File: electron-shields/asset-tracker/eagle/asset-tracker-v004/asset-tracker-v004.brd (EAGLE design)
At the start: 57.1 x 57.1 mm, 23 parts, among them J1 1X2-3.5MM, T1 DMG3415, U1 PAM-7Q-GPS-TH, U3 LIS3DHTR, X1 ELECTRON

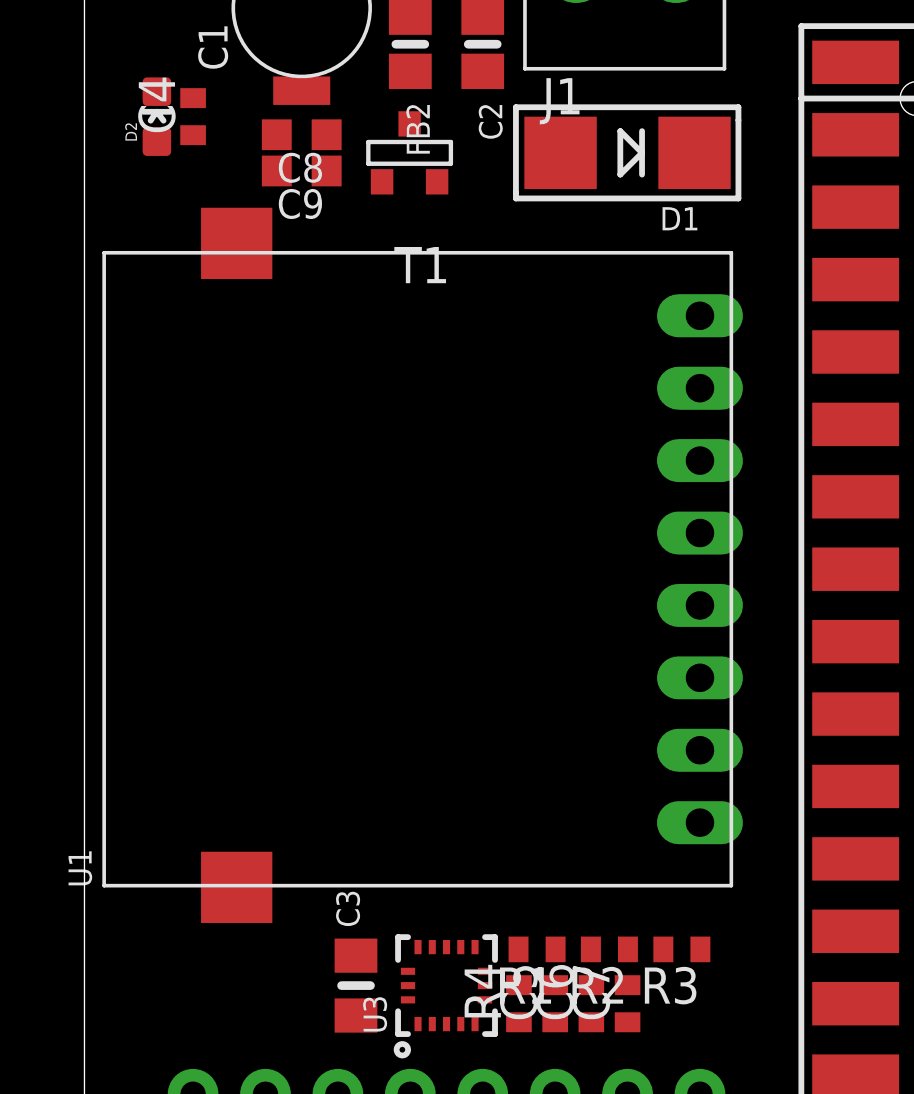
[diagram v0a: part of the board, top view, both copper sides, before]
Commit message: added max-m8 gps and max2674 ant switch packages
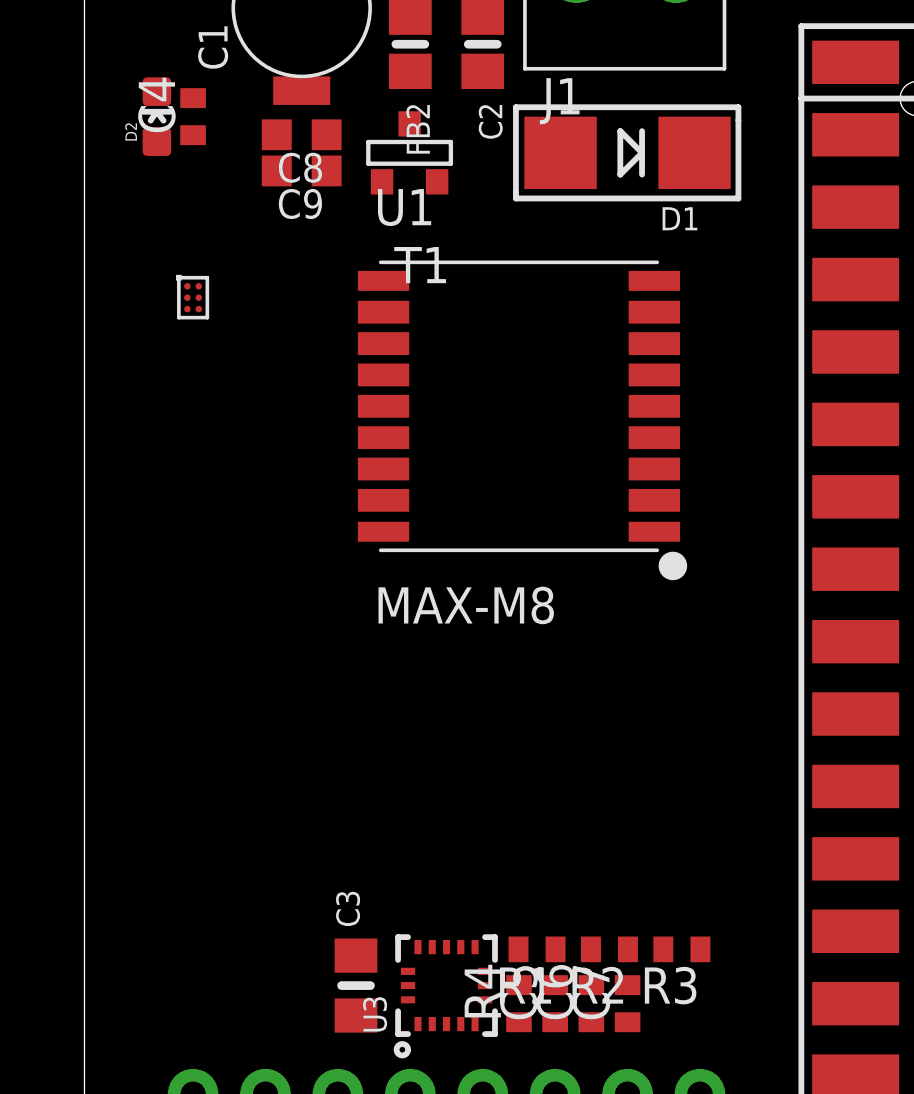
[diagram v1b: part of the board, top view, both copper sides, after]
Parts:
- added U2: MAX2674, maxim:WLP-6
- U1: value PAM-7Q-GPS-TH -> MAX-M8; device u-blox:PAM-7Q-TH -> u-blox:MAX-M8
- moved U1 15.9 mm to (15.2, 38.1), turned to 0 degrees
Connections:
- removed net V_BKP: U1.5
- new net GNDAC: U2.B2
- new net GNDDC: U2.C1
- net GND: no longer U1.3
- net VCC: now also U2.A1; no longer U1.4
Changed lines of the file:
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@@
 </autorouter>
 <elements>
-<element name="U1" library="u-blox" package="PAM-7Q-TH" value="PAM-7Q-GPS-TH" x="21.59" y="23.495" rot="R90"/>
 <element name="C1" library="adafruit" package="414-VA5R" value="" x="7.62" y="52.07" rot="R90"/>
 <element name="U3" library="microbuilder" package="LGA16_3X3MM" value="LIS3DHTR" x="12.7" y="17.78" rot="R90"/>
@@
 <element name="C8" library="rcl" package="C0603K" value="" x="7.62" y="47.625" rot="R180"/>
 <element name="C9" library="rcl" package="C0603K" value="" x="7.62" y="46.355" rot="R180"/>
+<element name="U1" library="u-blox" package="MAX-M8" value="MAX-M8" x="15.24" y="38.1"/>
+<element name="U2" library="maxim" package="WLP-6" value="MAX2674" x="3.81" y="41.91"/>
 </elements>
 <signals>
 <signal name="GND">
-<contactref element="U1" pad="3"/>
 <contactref element="U3" pad="5"/>
 <contactref element="U3" pad="10"/>
@@
 <contactref element="X1" pad="33B"/>
 <contactref element="X1" pad="33C"/>
-<wire x1="13.2" y1="19.13" x2="21.59" y2="28.575" width="0" layer="19" extent="1-1"/>
-<wire x1="12.2" y1="19.13" x2="13.2" y2="19.13" width="0" layer="19" extent="1-1"/>
-<wire x1="13.7" y1="16.43" x2="13.2" y2="19.13" width="0" layer="19" extent="1-1"/>
-<wire x1="9.525" y1="18.83" x2="13.7" y2="16.43" width="0" layer="19" extent="1-1"/>
-<wire x1="13.97" y1="49.85" x2="9.525" y2="18.83" width="0" layer="19" extent="1-1"/>
-<wire x1="17.25" y1="53.34" x2="13.97" y2="49.85" width="0" layer="19" extent="1-1"/>
-<wire x1="34.29" y1="47.625" x2="13.97" y2="49.85" width="0" layer="19" extent="1-1"/>
+<wire x1="47.371" y1="42.545" x2="51.689" y2="42.545" width="0" layer="19" extent="1-1"/>
+<wire x1="44.45" y1="42.545" x2="47.371" y2="42.545" width="0" layer="19" extent="1-1"/>
+<wire x1="34.29" y1="47.625" x2="44.45" y2="42.545" width="0" layer="19" extent="1-1"/>
 <wire x1="31.369" y1="47.625" x2="34.29" y2="47.625" width="0" layer="19" extent="1-1"/>
 <wire x1="27.051" y1="47.625" x2="31.369" y2="47.625" width="0" layer="19" extent="1-1"/>
-<wire x1="44.45" y1="42.545" x2="34.29" y2="47.625" width="0" layer="19" extent="1-1"/>
-<wire x1="47.371" y1="42.545" x2="44.45" y2="42.545" width="0" layer="19" extent="1-1"/>
-<wire x1="51.689" y1="42.545" x2="47.371" y2="42.545" width="0" layer="19" extent="1-1"/>
-</signal>
-<signal name="VCC">
-<contactref element="U1" pad="4"/>
-</signal>
-<signal name="V_BKP">
-<contactref element="U1" pad="5"/>
+<wire x1="17.25" y1="53.34" x2="27.051" y2="47.625" width="0" layer="19" extent="1-1"/>
+<wire x1="13.97" y1="49.85" x2="17.25" y2="53.34" width="0" layer="19" extent="1-1"/>
+<wire x1="13.2" y1="19.13" x2="13.97" y2="49.85" width="0" layer="19" extent="1-1"/>
+<wire x1="12.2" y1="19.13" x2="13.2" y2="19.13" width="0" layer="19" extent="1-1"/>
+<wire x1="9.525" y1="18.83" x2="12.2" y2="19.13" width="0" layer="19" extent="1-1"/>
+<wire x1="13.7" y1="16.43" x2="13.2" y2="19.13" width="0" layer="19" extent="1-1"/>
 </signal>
 <signal name="3.3V">
@@
 <wire x1="27.051" y1="50.165" x2="31.369" y2="50.165" width="0" layer="19" extent="1-1"/>
 </signal>
+<signal name="GNDAC">
+<contactref element="U2" pad="B2"/>
+</signal>
+<signal name="VCC">
+<contactref element="U2" pad="A1"/>
+</signal>
+<signal name="GNDDC">
+<contactref element="U2" pad="C1"/>
+</signal>
 </signals>

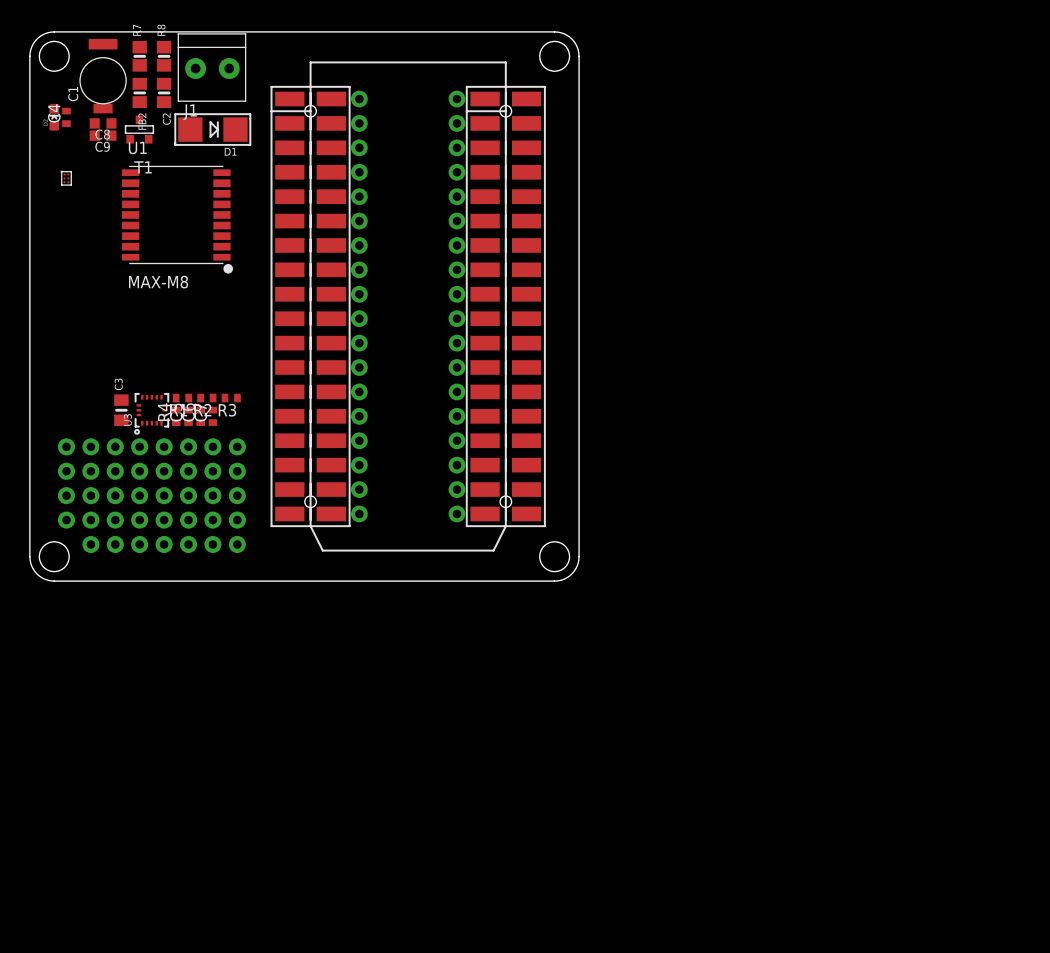
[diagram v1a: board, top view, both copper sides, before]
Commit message: updated schematic and added more data sheets
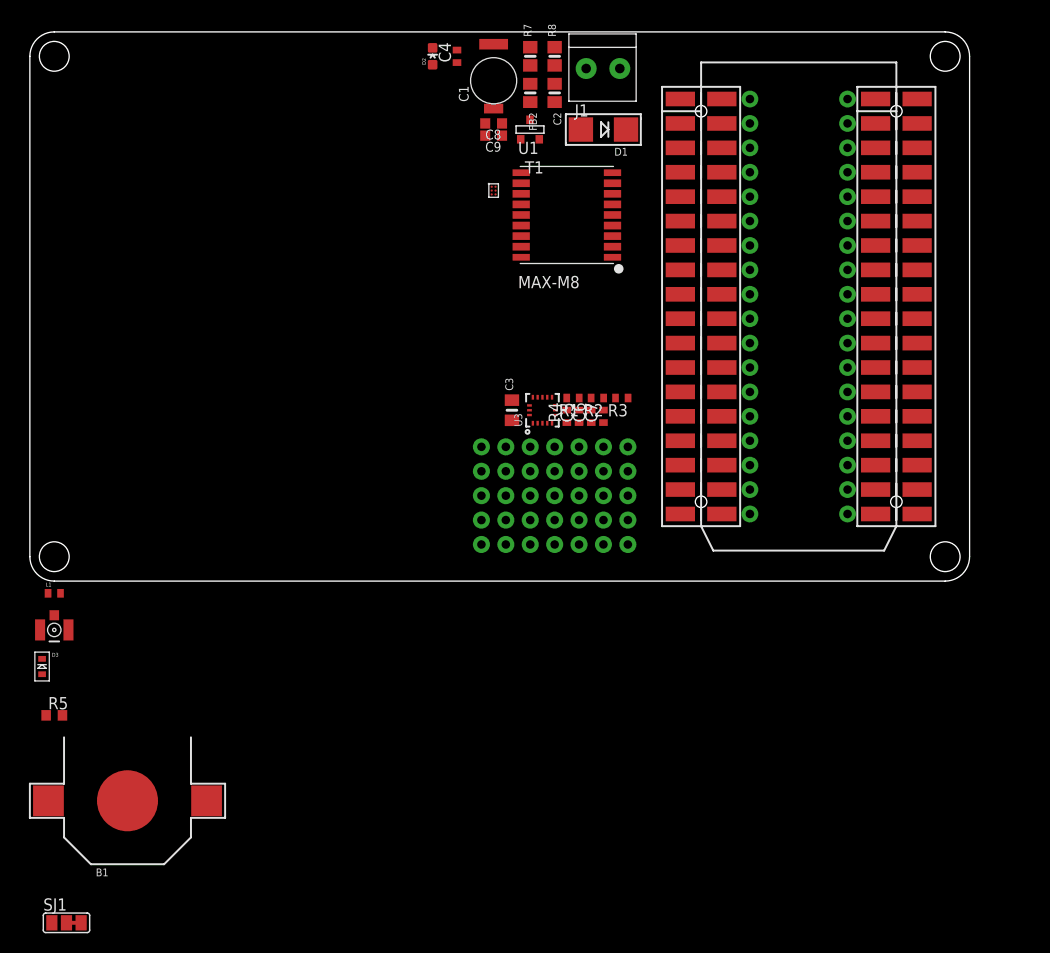
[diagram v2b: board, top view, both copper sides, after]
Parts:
- added B1: CR1220, microbuilder:CR1220
- added D3: (no value), adafruit:SOD-523
- added L1: (no value), Particle:C0402
- added R5: 270, rcl:R0603
- added SJ1: JUMPER-PAD-3-2OF3_NC_BY_TRACE_LARGE, SparkFun-Passives:PAD-JUMPER-3-2OF3_NC_BY_TRACE_YES_SILK_LARGE
- added X2: IPEX-20279-001E, Particle:IPEX-20279-001E
- C1: value (none) -> 60mF
- C5: value (none) -> 100pF
- moved U2 44.5 mm to (48.3, 40.6)
- moved C4 41.1 mm to (44.5, 54.6)
- moved X1 40.6 mm to (80.0, 28.6)
- moved C1 40.6 mm to (48.3, 52.1)
- moved C2 40.6 mm to (54.6, 50.8)
- moved C3 40.6 mm to (50.2, 17.8)
- moved C5 40.6 mm to (57.1, 17.1)
- moved C6 40.6 mm to (58.4, 17.1)
- moved C7 40.6 mm to (59.7, 17.1)
- moved C8 40.6 mm to (48.3, 47.6)
- moved C9 40.6 mm to (48.3, 46.4)
- moved D1 40.6 mm to (59.7, 47.0)
- moved FB2 40.6 mm to (52.1, 50.8)
- moved J1 40.6 mm to (59.7, 53.3)
- moved R1 40.6 mm to (56.5, 19.1)
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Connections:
- removed net 3V3: X1.36A, X1.36B, X1.36C
- removed net GNDAC: U2.B2
- removed net GNDDC: U2.C1
- removed net VCC: U2.A1
- removed net VIN: X1.1A, X1.1B, X1.1C
- new net GPS_!RESET: U1.9
- new net GPS_!SAFEBOOT: U1.18
- new net GPS_EXTINT: U1.5
- new net GPS_LNA_EN: U1.13
- new net GPS_PWR_EN: R7.1, T1.3, X1.31A, X1.31B, X1.31C
- new net GPS_RF_IN: C5.2, U1.11
- new net GPS_RXD: U1.3, X1.3A, X1.3B, X1.3C
- new net GPS_SCL: U1.17
- new net GPS_SDA: U1.16
- new net GPS_TXD: U1.2, X1.4A, X1.4B, X1.4C
- new net N$10: D3.K, R5.2
- new net N$11: B1.+$1, SJ1.1
- new net N$4: C5.1, U2.A2
- new net N$43: X1.6A, X1.6B, X1.6C
- new net N$48: X1.11A, X1.11B, X1.11C
- new net N$49: X1.12A, X1.12B, X1.12C
- new net N$5: U2.C2, X2.1
- new net N$57: X1.13A, X1.13B, X1.13C
- new net N$58: X1.14A, X1.14B, X1.14C
- new net N$59: X1.15A, X1.15B, X1.15C
- new net N$6: D2.C, R1.2
- new net N$60: X1.16A, X1.16B, X1.16C
- new net N$61: X1.17A, X1.17B, X1.17C
- new net N$62: X1.18A, X1.18B, X1.18C
- new net N$63: X1.19A, X1.19B, X1.19C
- new net N$64: X1.20A, X1.20B, X1.20C
- new net N$65: X1.21A, X1.21B, X1.21C
- new net N$66: X1.22A, X1.22B, X1.22C
- new net N$67: X1.23A, X1.23B, X1.23C
- new net N$68: X1.24A, X1.24B, X1.24C
- new net N$69: X1.25A, X1.25B, X1.25C
- new net N$7: C1.+, R5.1, SJ1.3
- new net N$70: X1.26A, X1.26B, X1.26C
- new net N$71: X1.27A, X1.27B, X1.27C
- new net N$72: X1.28A, X1.28B, X1.28C
- new net N$73: X1.29A, X1.29B, X1.29C
- new net N$74: X1.30A, X1.30B, X1.30C
- new net N$76: X1.32A, X1.32B, X1.32C
- new net N$78: X1.34A, X1.34B, X1.34C
- new net N$79: X1.35A, X1.35B, X1.35C
- new net TIMEPULSE: D2.A, U1.4
- new net VCC_RF: U1.14, U2.A1
- new net V_ANT: U1.15
- new net V_BCKP: SJ1.2, U1.6
- net 3.3V: now also D3.A, X1.36A, X1.36B, X1.36C
- net ACCEL_CS: now also X1.10A, X1.10B, X1.10C
- net ACCEL_INT1: now also X1.5A, X1.5B, X1.5C
- net ACCEL_MISO: now also X1.8A, X1.8B, X1.8C
- net ACCEL_MOSI: now also X1.7A, X1.7B, X1.7C
- net ACCEL_SCK: now also X1.9A, X1.9B, X1.9C
- net GND: now also B1.-, C1.-, C4.1, C9.1, R1.1, U1.1, U1.10, U1.12, U2.B2, U2.C1, X2.2@1, X2.2@2
- net N$1: now also C4.2, C9.2, U1.7, U1.8; no longer FB2.2
- net N$2: now also L1.2, U2.B1; no longer FB2.1
- net N$3: now also C6.2, L1.1; no longer R7.1, T1.3
- net N$8: now also X1.1A, X1.1B, X1.1C
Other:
- board size 57.1 x 57.1 mm -> 97.8 x 57.1 mm

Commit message: added patch antenna and enclosure outline
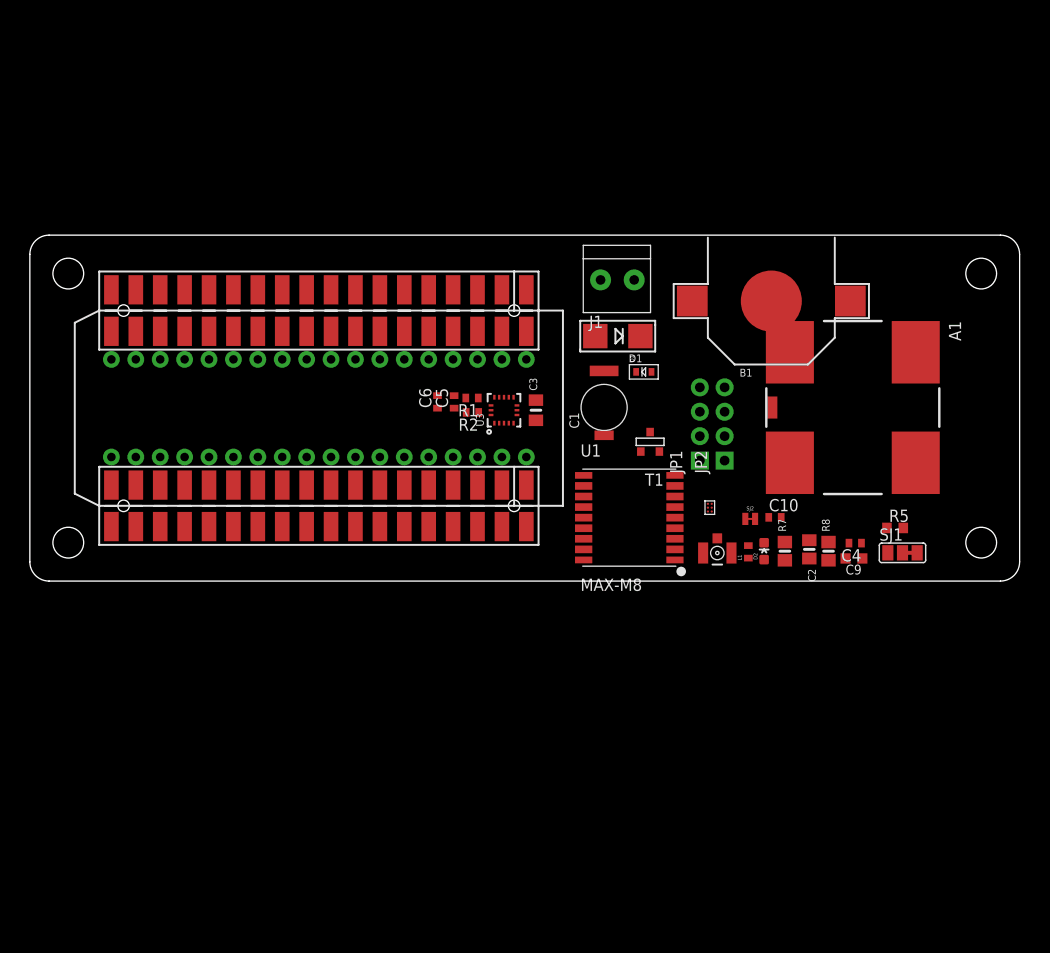
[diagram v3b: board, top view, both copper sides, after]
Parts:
- removed C7: (no value), rcl:C0402
- removed C8: (no value), rcl:C0603K
- removed FB2: Ferrite, microbuilder:0805-NO@1
- removed R3, R4: (no value), rcl:R0402
- added A1: GPS-ANTENNA, antenna:ANT1818B00BT1516S
- added C10: 0.1uF, rcl:C0402
- added JP1, JP2: (no value), SparkFun-Connectors:1X04_NO_SILK
- added SJ2: JUMPER-PAD-2-NC_BY_TRACENO_SILK, SparkFun-Passives:PAD-JUMPER-2-NC_BY_TRACE_NO_SILK
- C4: value (none) -> 0.1uF
- C6: value (none) -> 100pF
- C9: value (none) -> 10uF
- L1: value (none) -> 88nH
- R2: value (none) -> 100K
- moved SJ1 95.1 mm to (90.8, 2.94)
- moved R5 89.6 mm to (90.0, 5.53)
- moved B1 84.8 mm to (77.2, 29.1)
- moved L1 72.4 mm to (74.8, 3.04), turned to 90 degrees
- moved D3 69.7 mm to (63.9, 21.8), turned to 90 degrees
- moved X2 69.5 mm to (71.5, 2.92)
- moved C4 65.4 mm to (85.9, 3.95), turned to 180 degrees
- moved D2 62.0 mm to (76.4, 3.11)
- moved R8 58.9 mm to (83.1, 3.11)
- moved R7 57.9 mm to (78.6, 3.11)
- moved C9 57.8 mm to (85.8, 2.36)
- moved C2 54.4 mm to (81.1, 3.30)
- moved X1 51.0 mm to (30.1, 18.0), turned to 270 degrees
- moved U2 39.9 mm to (70.8, 7.64)
- moved C1 35.9 mm to (59.8, 18.1)
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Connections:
- removed net N$43: X1.6A, X1.6B, X1.6C
- removed net N$48: X1.11A, X1.11B, X1.11C
- removed net N$49: X1.12A, X1.12B, X1.12C
- removed net N$57: X1.13A, X1.13B, X1.13C
- removed net N$58: X1.14A, X1.14B, X1.14C
- removed net N$59: X1.15A, X1.15B, X1.15C
- removed net N$60: X1.16A, X1.16B, X1.16C
- removed net N$61: X1.17A, X1.17B, X1.17C
- removed net N$62: X1.18A, X1.18B, X1.18C
- removed net N$63: X1.19A, X1.19B, X1.19C
- removed net N$64: X1.20A, X1.20B, X1.20C
- removed net N$65: X1.21A, X1.21B, X1.21C
- removed net N$66: X1.22A, X1.22B, X1.22C
- removed net N$67: X1.23A, X1.23B, X1.23C
- removed net N$68: X1.24A, X1.24B, X1.24C
- removed net N$69: X1.25A, X1.25B, X1.25C
- removed net N$70: X1.26A, X1.26B, X1.26C
- removed net N$71: X1.27A, X1.27B, X1.27C
- removed net N$72: X1.28A, X1.28B, X1.28C
- removed net N$73: X1.29A, X1.29B, X1.29C
- removed net N$74: X1.30A, X1.30B, X1.30C
- removed net N$76: X1.32A, X1.32B, X1.32C
- removed net N$78: X1.34A, X1.34B, X1.34C
- removed net N$79: X1.35A, X1.35B, X1.35C
- new net A0: JP1.1, X1.12A, X1.12B, X1.12C
- new net A1: JP1.2, X1.11A, X1.11B, X1.11C
- new net GPS_VCC: C4.2, C9.2, R2.2, T1.1, U1.7, U1.8
- new net N$12: A1.ANT, C6.1
- new net SCL: JP2.1, X1.26A, X1.26B, X1.26C
- new net SDA: JP2.2, X1.25A, X1.25B, X1.25C
- net 3.3V: now also JP1.3, JP2.3, SJ2.2; no longer D3.A
- net GND: now also C10.1, JP1.4, JP2.4
- net GPS_!RESET: now also R2.1
- net N$1: now also D3.A, SJ2.1; no longer C4.2, C9.2, T1.1, U1.7, U1.8
- net VCC_RF: now also C10.2
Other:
- board size 97.8 x 57.1 mm -> 103 x 36 mm
